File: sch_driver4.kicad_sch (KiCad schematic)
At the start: 19 parts, among them Q4 PSMN4R0-30YLDX, U14 TS5A3159ADCK, U2 ADA4099-2xR, U24 OPA365AIDBV, U6 ADA4099-1

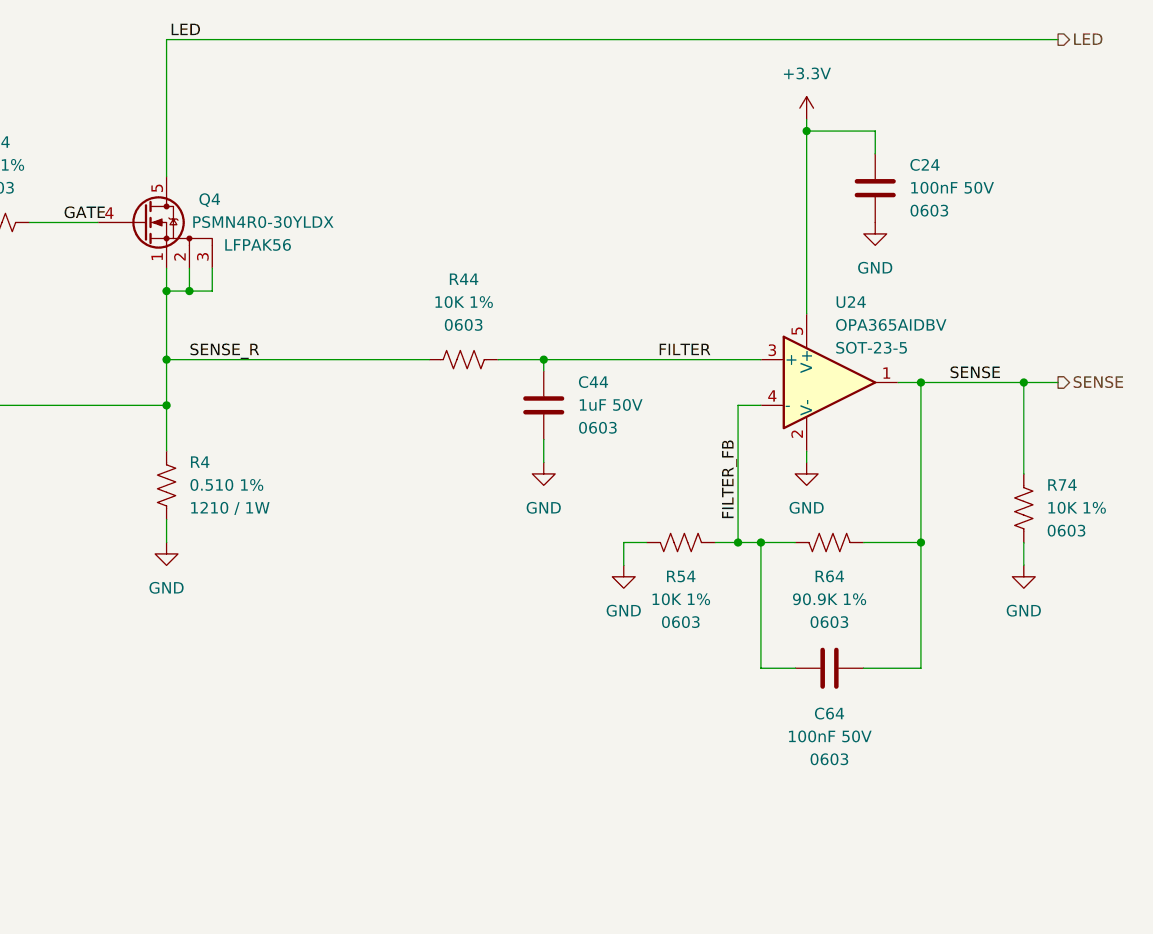
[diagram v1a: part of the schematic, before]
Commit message: Initial placement on 45 x 30 mm outline. Dropped sense apms. Switch to two 2x6 connectors.
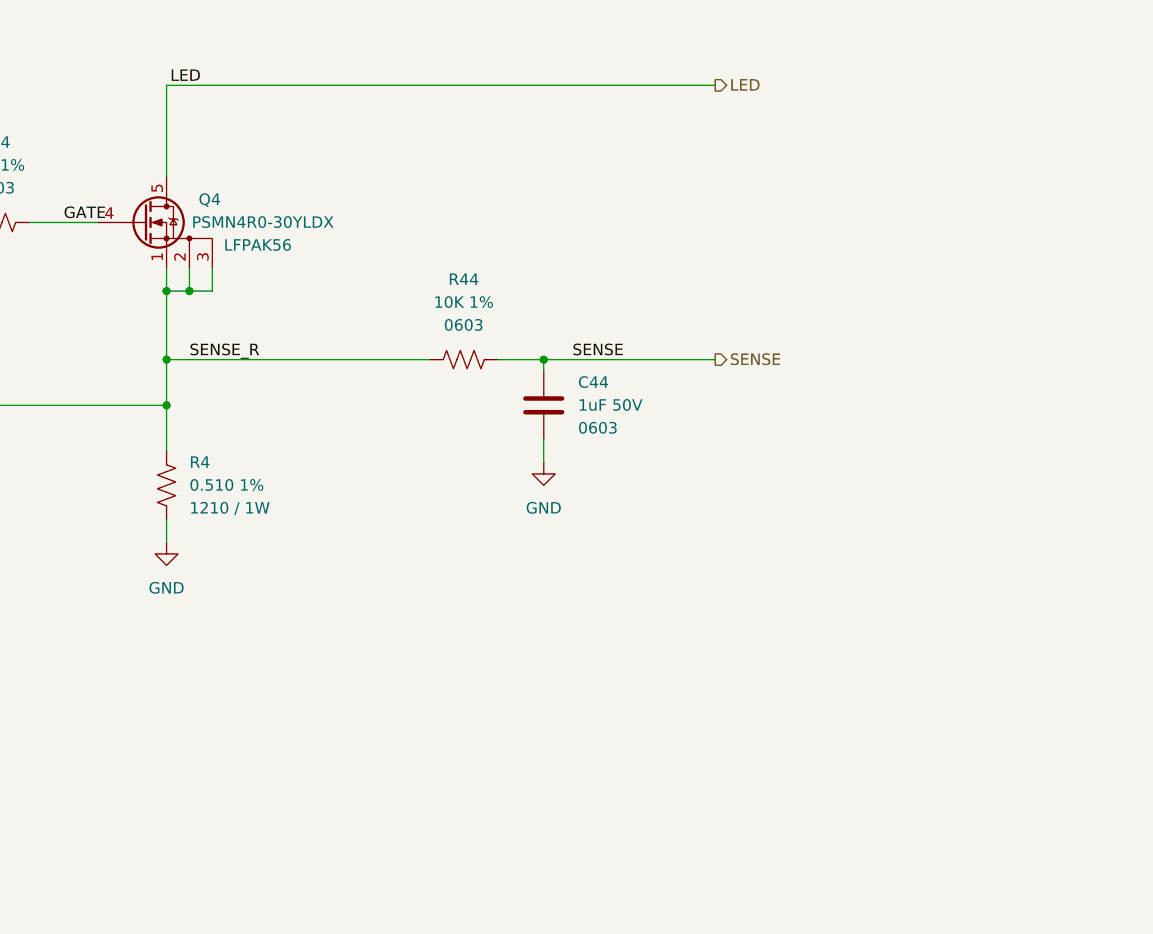
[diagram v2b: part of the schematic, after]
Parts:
- removed C24, C64: 100nF 50V, $Local:C_0603_1608Metric, symbol $Local:C_0603_100NF_50V
- removed R54, R74: 10K 1%, $Local:R_0603_1608Metric, symbol $Local:R_0603_10K
- removed R64: 90.9K 1%, $Local:R_0603_1608Metric, symbol $Local:R_0603_10K
- removed U24: OPA365AIDBV, $Local:SOT-23-5, symbol $Local:OPA365AIDBV
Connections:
- net FILTER is gone; now on net SENSE: C44.1, R44.1
